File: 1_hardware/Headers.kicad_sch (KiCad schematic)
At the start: 2 parts, among them J111 SSW-132-24-L-D, J121 SSW-132-24-L-D

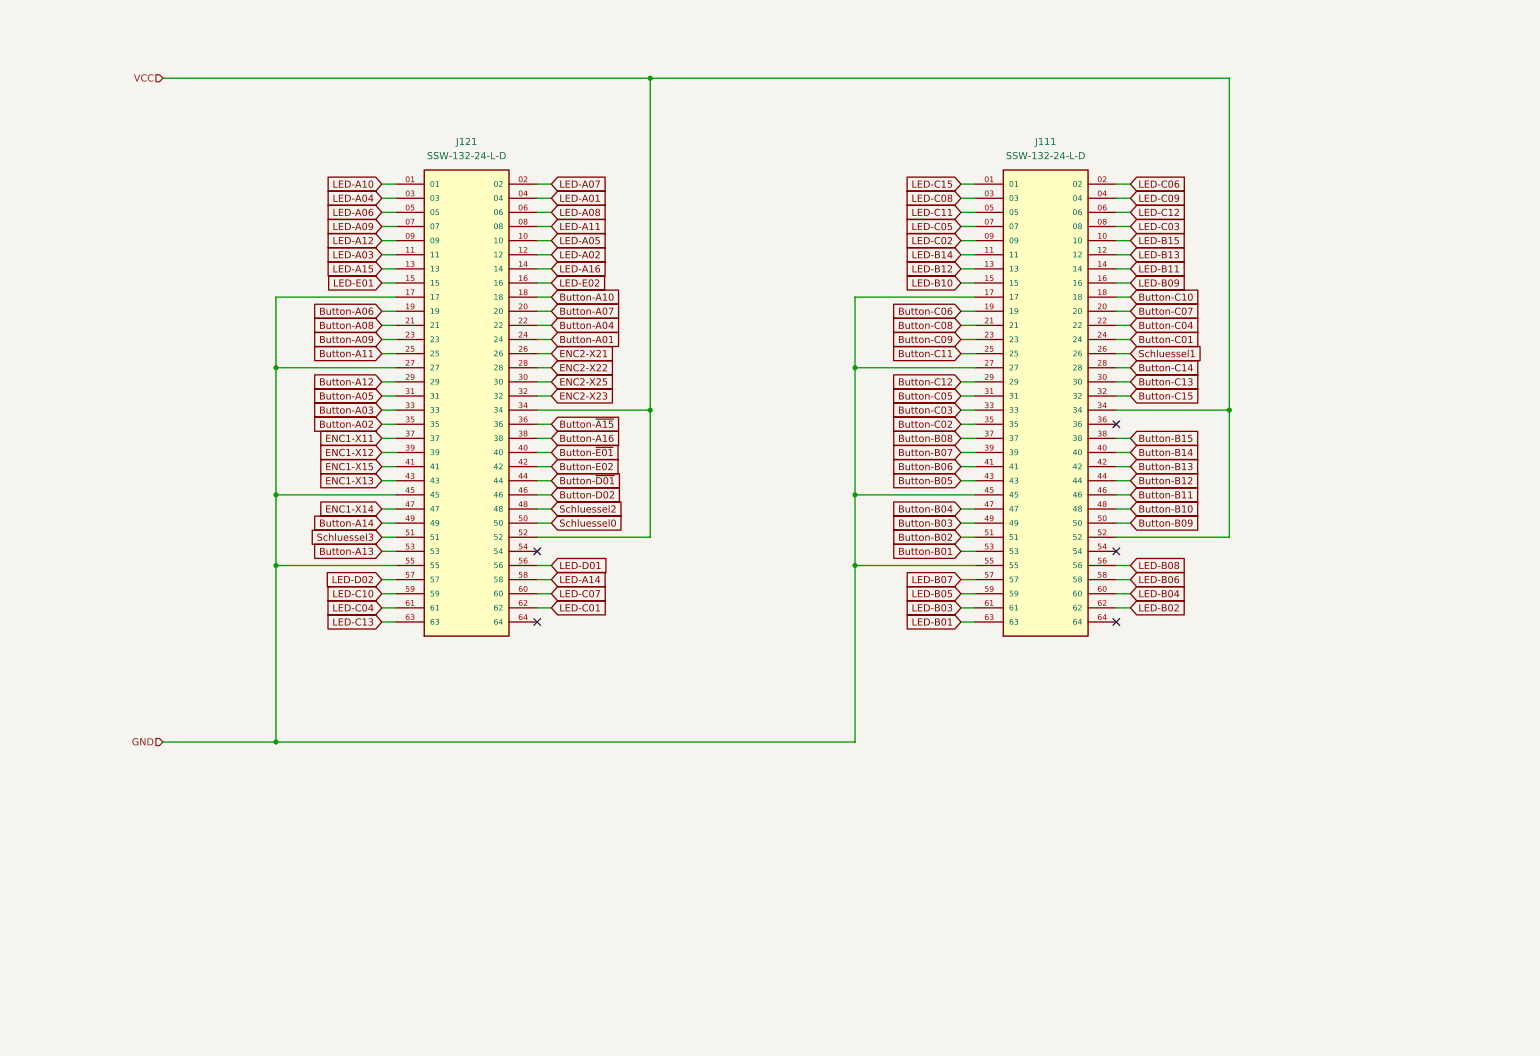
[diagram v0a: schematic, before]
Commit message: finished most of schematic, init STM32 program
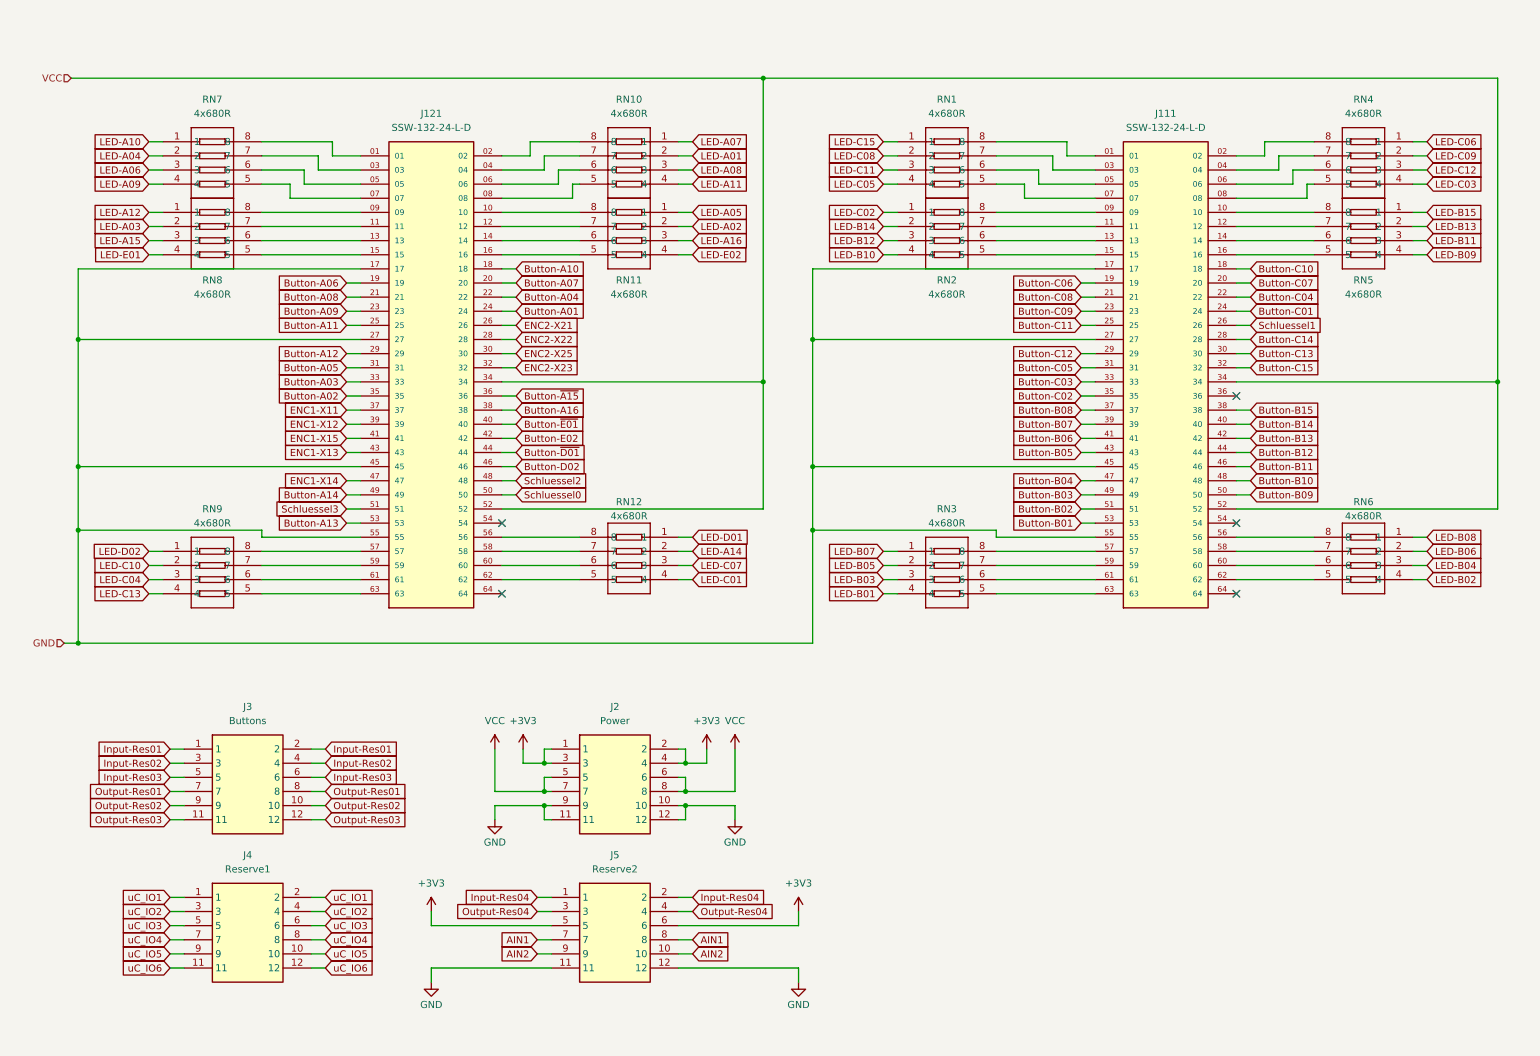
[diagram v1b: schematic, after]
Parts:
- added J2: Power, CostumLibrary:1824460000 - LSF-SMT 3.500690 3.5SN BK TU, symbol CostumLibrary:1824460000 - LSF-SMT 3.50/06/90 3.5SN BK TU
- added J3: Buttons, CostumLibrary:1824460000 - LSF-SMT 3.500690 3.5SN BK TU, symbol CostumLibrary:1824460000 - LSF-SMT 3.50/06/90 3.5SN BK TU
- added J4: Reserve1, CostumLibrary:1824460000 - LSF-SMT 3.500690 3.5SN BK TU, symbol CostumLibrary:1824460000 - LSF-SMT 3.50/06/90 3.5SN BK TU
- added J5: Reserve2, CostumLibrary:1824460000 - LSF-SMT 3.500690 3.5SN BK TU, symbol CostumLibrary:1824460000 - LSF-SMT 3.50/06/90 3.5SN BK TU
- added RN1, RN10, RN11, RN12, RN2, RN3, RN4, RN5, RN6, RN7, RN8, RN9: 4x680R, easyeda2kicad:RES-ARRAY-SMD_0603-8P-L3.2-W1.6-BL, symbol easyeda2kicad:4D03WGJ0681T5E
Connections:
- net GND: now also J2.10, J2.11, J2.12, J2.9, J5.11, J5.12
- net LED-A01: now also RN10.2; no longer J121.04
- net LED-A02: now also RN11.2; no longer J121.12
- net LED-A03: now also RN8.2; no longer J121.11
- net LED-A04: now also RN7.2; no longer J121.03
- net LED-A05: now also RN11.1; no longer J121.10
- net LED-A06: now also RN7.3; no longer J121.05
- net LED-A07: now also RN10.1; no longer J121.02
- net LED-A08: now also RN10.3; no longer J121.06
- net LED-A09: now also RN7.4; no longer J121.07
- net LED-A10: now also RN7.1; no longer J121.01
- net LED-A11: now also RN10.4; no longer J121.08
- net LED-A12: now also RN8.1; no longer J121.09
- net LED-A14: now also RN12.2; no longer J121.58
- net LED-A15: now also RN8.3; no longer J121.13
- net LED-A16: now also RN11.3; no longer J121.14
- net LED-B01: now also RN3.4; no longer J111.63
- net LED-B02: now also RN6.4; no longer J111.62
- net LED-B03: now also RN3.3; no longer J111.61
- net LED-B04: now also RN6.3; no longer J111.60
- net LED-B05: now also RN3.2; no longer J111.59
- net LED-B06: now also RN6.2; no longer J111.58
- net LED-B07: now also RN3.1; no longer J111.57
- net LED-B08: now also RN6.1; no longer J111.56
- net LED-B09: now also RN5.4; no longer J111.16
- net LED-B10: now also RN2.4; no longer J111.15
- net LED-B11: now also RN5.3; no longer J111.14
- net LED-B12: now also RN2.3; no longer J111.13
- net LED-B13: now also RN5.2; no longer J111.12
- net LED-B14: now also RN2.2; no longer J111.11
- net LED-B15: now also RN5.1; no longer J111.10
- net LED-C01: now also RN12.4; no longer J121.62
- net LED-C02: now also RN2.1; no longer J111.09
- net LED-C03: now also RN4.4; no longer J111.08
- net LED-C04: now also RN9.3; no longer J121.61
- net LED-C05: now also RN1.4; no longer J111.07
- net LED-C06: now also RN4.1; no longer J111.02
- net LED-C07: now also RN12.3; no longer J121.60
- net LED-C08: now also RN1.2; no longer J111.03
- net LED-C09: now also RN4.2; no longer J111.04
- net LED-C10: now also RN9.2; no longer J121.59
- net LED-C11: now also RN1.3; no longer J111.05
- net LED-C12: now also RN4.3; no longer J111.06
- net LED-C13: now also RN9.4; no longer J121.63
- net LED-C15: now also RN1.1; no longer J111.01
- net LED-D01: now also RN12.1; no longer J121.56
- net LED-D02: now also RN9.1; no longer J121.57
- net LED-E01: now also RN8.4; no longer J121.15
- net LED-E02: now also RN11.4; no longer J121.16
- net VCC: now also J2.5, J2.6, J2.7, J2.8
- new net: J121.15, RN8.5
- new net: J121.13, RN8.6
- new net: J121.11, RN8.7
- new net: J121.09, RN8.8
- new net: J121.08, RN10.5
- new net: J121.06, RN10.6
- new net: J121.04, RN10.7
- new net: J121.02, RN10.8
- new net: J121.16, RN11.5
- new net: J121.14, RN11.6
- new net: J121.12, RN11.7
- new net: J121.10, RN11.8
- new net: J121.07, RN7.5
- new net: J121.05, RN7.6
- new net: J121.03, RN7.7
- new net: J121.01, RN7.8
- new net: J121.62, RN12.5
- new net: J121.60, RN12.6
- new net: J121.58, RN12.7
- new net: J121.56, RN12.8
- new net: J111.16, RN5.5
- new net: J111.14, RN5.6
- new net: J111.12, RN5.7
- new net: J111.10, RN5.8
- new net: J121.57, RN9.8
- new net: J121.59, RN9.7
- new net: J121.61, RN9.6
- new net: J121.63, RN9.5
- new net: J111.15, RN2.5
- new net: J111.13, RN2.6
- new net: J111.11, RN2.7
- new net: J111.09, RN2.8
- new net: J111.08, RN4.5
- new net: J111.06, RN4.6
- new net: J111.04, RN4.7
- new net: J111.02, RN4.8
- new net: J111.62, RN6.5
- new net: J111.60, RN6.6
- new net: J111.58, RN6.7
- new net: J111.56, RN6.8
- new net: J111.07, RN1.5
- new net: J111.05, RN1.6
- new net: J111.03, RN1.7
- new net: J111.01, RN1.8
- new net: J111.63, RN3.5
- new net: J111.61, RN3.6
- new net: J111.59, RN3.7
- new net: J111.57, RN3.8
- new net +3V3: J2.1, J2.2, J2.3, J2.4, J5.5, J5.6
- new net AIN1: J5.7, J5.8
- new net AIN2: J5.10, J5.9
- new net Input-Res01: J3.1, J3.2
- new net Input-Res02: J3.3, J3.4
- new net Input-Res03: J3.5, J3.6
- new net Input-Res04: J5.1, J5.2
- new net Output-Res01: J3.7, J3.8
- new net Output-Res02: J3.10, J3.9
- new net Output-Res03: J3.11, J3.12
- new net Output-Res04: J5.3, J5.4
- new net uC_IO1: J4.1, J4.2
- new net uC_IO2: J4.3, J4.4
- new net uC_IO3: J4.5, J4.6
- new net uC_IO4: J4.7, J4.8
- new net uC_IO5: J4.10, J4.9
- new net uC_IO6: J4.11, J4.12
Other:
- moved on the sheet: J111, J121

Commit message: finished schematics and board
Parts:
- removed J4: Reserve1, CostumLibrary:1824460000 - LSF-SMT 3.500690 3.5SN BK TU, symbol CostumLibrary:1824460000 - LSF-SMT 3.50/06/90 3.5SN BK TU
- renumbered J5 to J4
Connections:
- net LED-A01: now also RN7.5; no longer RN10.2
- net LED-A02: now also RN9.5; no longer RN11.2
- net LED-A03: now also RN9.6; no longer RN8.2
- net LED-A04: now also RN7.6; no longer RN7.2
- net LED-A05: now also RN9.7; no longer RN11.1
- net LED-A06: now also RN8.8; no longer RN7.3
- net LED-A07: now also RN7.7; no longer RN10.1
- net LED-A08: now also RN8.7; no longer RN10.3
- net LED-A09: now also RN8.6; no longer RN7.4
- net LED-A10: now also RN7.8; no longer RN7.1
- net LED-A11: now also RN8.5; no longer RN10.4
- net LED-A12: now also RN9.8; no longer RN8.1
- net LED-A14: now also RN11.6; no longer RN12.2
- net LED-A15: now also RN10.8; no longer RN8.3
- net LED-A16: now also RN10.7; no longer RN11.3
- net LED-B01: now also RN6.5; no longer RN3.4
- net LED-B02: now also RN6.6; no longer RN6.4
- net LED-B03: now also RN6.7; no longer RN3.3
- net LED-B04: now also RN6.8; no longer RN6.3
- net LED-B05: now also RN5.5; no longer RN3.2
- net LED-B06: now also RN5.6; no longer RN6.2
- net LED-B07: now also RN5.7; no longer RN3.1
- net LED-B08: now also RN5.8; no longer RN6.1
- net LED-B09: now also RN4.5; no longer RN5.4
- net LED-B10: now also RN4.6; no longer RN2.4
- net LED-B11: now also RN4.7; no longer RN5.3
- net LED-B12: now also RN4.8; no longer RN2.3
- net LED-B13: now also RN3.5; no longer RN5.2
- net LED-B14: now also RN3.6; no longer RN2.2
- net LED-B15: now also RN3.7; no longer RN5.1
- net LED-C01: now also RN12.6; no longer RN12.4
- net LED-C02: now also RN3.8; no longer RN2.1
- net LED-C03: now also RN2.5; no longer RN4.4
- net LED-C04: now also RN12.7; no longer RN9.3
- net LED-C05: now also RN2.6; no longer RN1.4
- net LED-C06: now also RN1.7; no longer RN4.1
- net LED-C07: now also RN12.8; no longer RN12.3
- net LED-C08: now also RN1.6; no longer RN1.2
- net LED-C09: now also RN1.5; no longer RN4.2
- net LED-C10: now also RN11.5; no longer RN9.2
- net LED-C11: now also RN2.8; no longer RN1.3
- net LED-C12: now also RN2.7; no longer RN4.3
- net LED-C13: now also RN12.5; no longer RN9.4
- net LED-C15: now also RN1.8; no longer RN1.1
- net LED-D01: now also RN11.8; no longer RN12.1
- net LED-D02: now also RN11.7; no longer RN9.1
- net LED-E01: now also RN10.6; no longer RN8.4
- net LED-E02: now also RN10.5; no longer RN11.4
- net P2.15: now reaches J121.15
- net P2.15: now also RN10.3; no longer RN8.5
- net P2.13: now reaches J121.13
- net P2.13: now also RN10.1; no longer RN8.6
- net P2.11: now reaches J121.11
- net P2.11: now also RN9.3; no longer RN8.7
- net P2.09: now reaches J121.09
- net P2.09: now also RN9.1; no longer RN8.8
- net P2.08: now reaches J121.08
- net P2.08: now also RN8.4; no longer RN10.5
- net P2.06: now reaches J121.06
- net P2.06: now also RN8.2; no longer RN10.6
- net P2.04: now reaches J121.04
- net P2.04: now also RN7.4; no longer RN10.7
- net P2.02: now reaches J121.02
- net P2.02: now also RN7.2; no longer RN10.8
- net P2.16: now reaches J121.16
- net P2.16: now also RN10.4; no longer RN11.5
- net P2.14: now reaches J121.14
- net P2.14: now also RN10.2; no longer RN11.6
- net P2.12: now reaches J121.12
- net P2.12: now also RN9.4; no longer RN11.7
- net P2.10: now reaches J121.10
- net P2.10: now also RN9.2; no longer RN11.8
- net P2.07: now reaches J121.07
- net P2.07: now also RN8.3; no longer RN7.5
- net P2.05: now reaches J121.05
- net P2.05: now also RN8.1; no longer RN7.6
- net P2.03: now reaches J121.03
- net P2.03: now also RN7.3; no longer RN7.7
- net P2.01: now reaches J121.01
- net P2.01: now also RN7.1; no longer RN7.8
- net P2.62: now reaches J121.62
- net P2.62: now also RN12.3; no longer RN12.5
- net P2.60: now reaches J121.60
- net P2.60: now also RN12.1; no longer RN12.6
- net P2.58: now reaches J121.58
- net P2.58: now also RN11.3; no longer RN12.7
- net P2.56: now reaches J121.56
- net P2.56: now also RN11.1; no longer RN12.8
- net P1.16: now reaches J111.16
- net P1.16: now also RN4.4; no longer RN5.5
- net P1.14: now reaches J111.14
- net P1.14: now also RN4.2; no longer RN5.6
- net P1.12: now reaches J111.12
- net P1.12: now also RN3.4; no longer RN5.7
- net P1.10: now reaches J111.10
- net P1.10: now also RN3.2; no longer RN5.8
- net P2.57: now reaches J121.57
- net P2.57: now also RN11.2; no longer RN9.8
- net P2.59: now reaches J121.59
- net P2.59: now also RN11.4; no longer RN9.7
- net P2.61: now reaches J121.61
- net P2.61: now also RN12.2; no longer RN9.6
- net P2.63: now reaches J121.63
- net P2.63: now also RN12.4; no longer RN9.5
- net P1.15: now reaches J111.15
- net P1.15: now also RN4.3; no longer RN2.5
- net P1.13: now reaches J111.13
- net P1.13: now also RN4.1; no longer RN2.6
- net P1.11: now reaches J111.11
- net P1.11: now also RN3.3; no longer RN2.7
- net P1.09: now reaches J111.09
- net P1.09: now also RN3.1; no longer RN2.8
- net P1.08: now reaches J111.08
- net P1.08: now also RN2.4; no longer RN4.5
- net P1.06: now reaches J111.06
- net P1.06: now also RN2.2; no longer RN4.6
- net P1.04: now reaches J111.04
- net P1.04: now also RN1.4; no longer RN4.7
- net P1.02: now reaches J111.02
- net P1.02: now also RN1.2; no longer RN4.8
- net P1.62: now reaches J111.62
- net P1.62: now also RN6.3; no longer RN6.5
- net P1.60: now reaches J111.60
- net P1.60: now also RN6.1; no longer RN6.6
- net P1.58: now reaches J111.58
- net P1.58: now also RN5.3; no longer RN6.7
- net P1.56: now reaches J111.56
- net P1.56: now also RN5.1; no longer RN6.8
- net P1.07: now reaches J111.07
- net P1.07: now also RN2.3; no longer RN1.5
- net P1.05: now reaches J111.05
- net P1.05: now also RN2.1; no longer RN1.6
- net P1.03: now reaches J111.03
- net P1.03: now also RN1.3; no longer RN1.7
- net P1.01: now reaches J111.01
- net P1.01: now also RN1.1; no longer RN1.8
- net P1.63: now reaches J111.63
- net P1.63: now also RN6.4; no longer RN3.5
- net P1.61: now reaches J111.61
- net P1.61: now also RN6.2; no longer RN3.6
- net P1.59: now reaches J111.59
- net P1.59: now also RN5.4; no longer RN3.7
- net P1.57: now reaches J111.57
- net P1.57: now also RN5.2; no longer RN3.8
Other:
- moved on the sheet: J111, J121, J2, J3, J4
